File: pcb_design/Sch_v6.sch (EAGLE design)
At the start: 33 parts

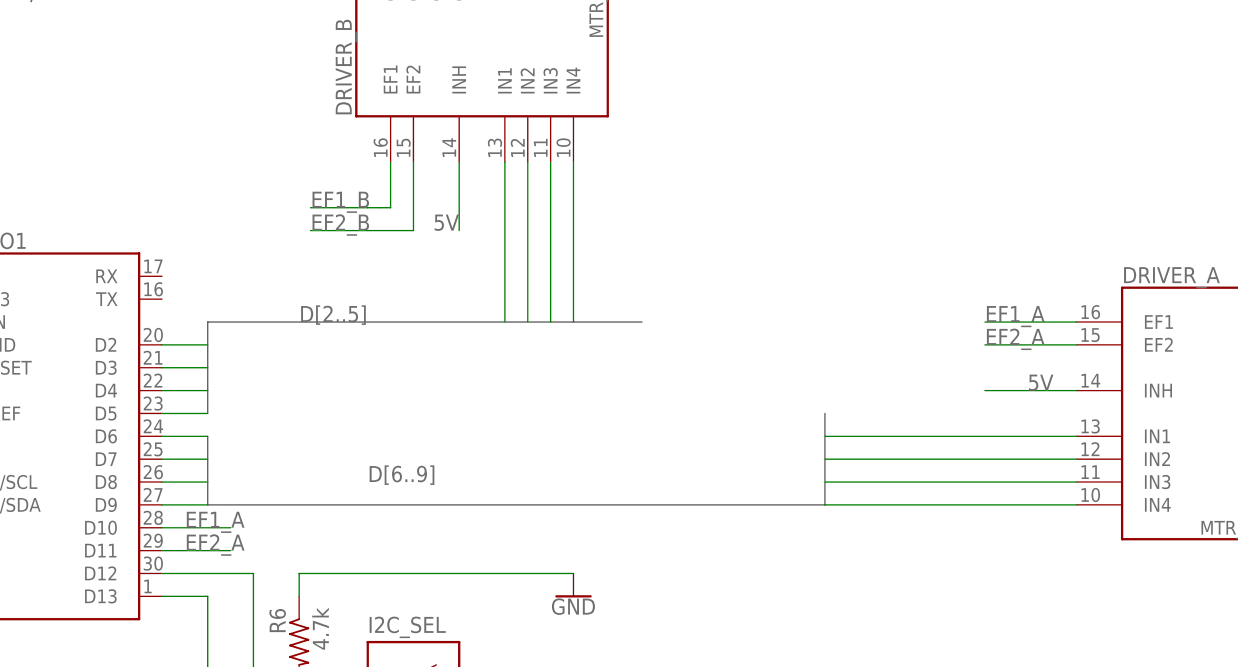
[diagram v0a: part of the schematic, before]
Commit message: removed old files and updated with CAM files for both pcbs.
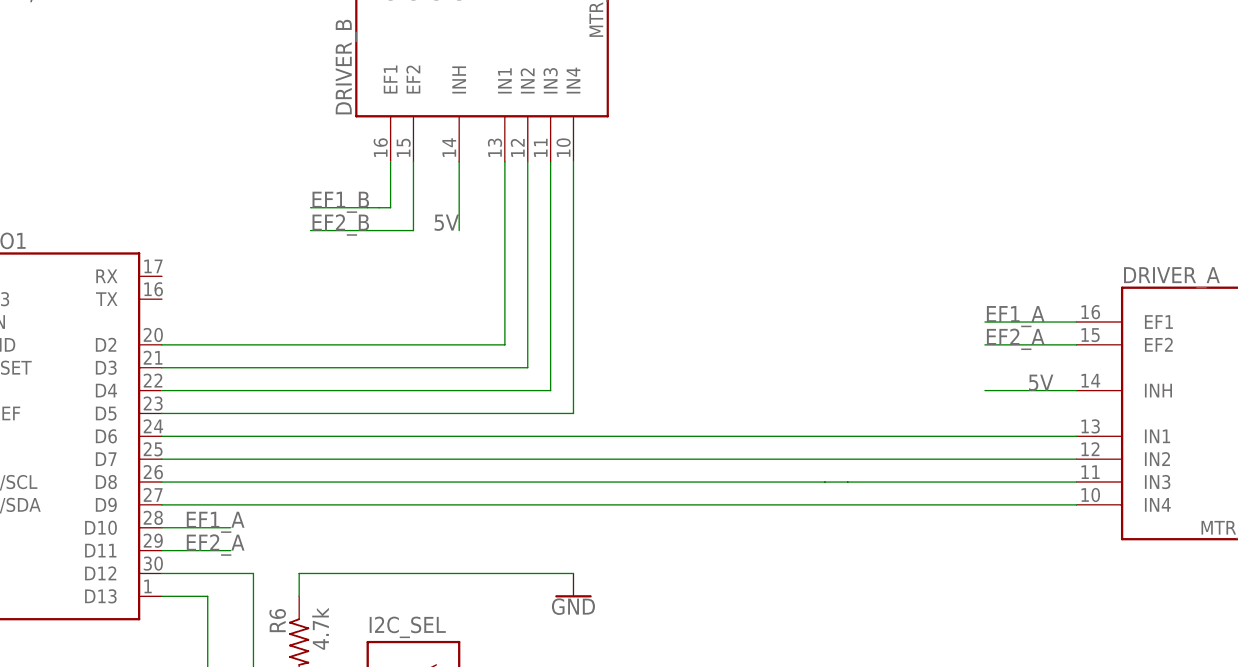
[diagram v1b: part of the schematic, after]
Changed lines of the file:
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@@
-</segment>
-</bus>
-<bus name="D[6..9]">
-<segment>
-<wire x1="53.34" y1="104.14" x2="53.34" y2="96.52" width="0.762" layer="92"/>
-<wire x1="53.34" y1="96.52" x2="121.92" y2="96.52" width="0.762" layer="92"/>
-<wire x1="121.92" y1="96.52" x2="121.92" y2="106.68" width="0.762" layer="92"/>
-<label x="71.12" y="99.06" size="1.778" layer="95"/>
-</segment>
-</bus>
-<bus name="D[2..5]">
-<segment>
-<wire x1="53.34" y1="106.68" x2="53.34" y2="116.84" width="0.762" layer="92"/>
-<wire x1="53.34" y1="116.84" x2="101.6" y2="116.84" width="0.762" layer="92"/>
-<label x="63.5" y="116.84" size="1.778" layer="95"/>
 </segment>
 </bus>
@@
 <net name="D6" class="0">
 <segment>
-<wire x1="149.86" y1="104.14" x2="121.92" y2="104.14" width="0.1524" layer="91"/>
+<pinref part="NANO1" gate="NANO_EVERY" pin="D6"/>
 <pinref part="DRIVER_A" gate="G$1" pin="IN1"/>
-</segment>
-<segment>
-<wire x1="48.26" y1="104.14" x2="53.34" y2="104.14" width="0.1524" layer="91"/>
-<pinref part="NANO1" gate="NANO_EVERY" pin="D6"/>
+<wire x1="48.26" y1="104.14" x2="149.86" y2="104.14" width="0.1524" layer="91"/>
 </segment>
 </net>
 <net name="D7" class="0">
 <segment>
-<wire x1="149.86" y1="101.6" x2="121.92" y2="101.6" width="0.1524" layer="91"/>
+<pinref part="NANO1" gate="NANO_EVERY" pin="D7"/>
 <pinref part="DRIVER_A" gate="G$1" pin="IN2"/>
-</segment>
-<segment>
-<wire x1="48.26" y1="101.6" x2="53.34" y2="101.6" width="0.1524" layer="91"/>
-<pinref part="NANO1" gate="NANO_EVERY" pin="D7"/>
+<wire x1="48.26" y1="101.6" x2="149.86" y2="101.6" width="0.1524" layer="91"/>
 </segment>
 </net>
 <net name="D8" class="0">
 <segment>
-<wire x1="149.86" y1="99.06" x2="121.92" y2="99.06" width="0.1524" layer="91"/>
+<pinref part="NANO1" gate="NANO_EVERY" pin="D8"/>
+<wire x1="149.86" y1="99.06" x2="124.46" y2="99.06" width="0.1524" layer="91"/>
 <pinref part="DRIVER_A" gate="G$1" pin="IN3"/>
-</segment>
-<segment>
-<wire x1="48.26" y1="99.06" x2="53.34" y2="99.06" width="0.1524" layer="91"/>
-<pinref part="NANO1" gate="NANO_EVERY" pin="D8"/>
+<wire x1="124.46" y1="99.06" x2="121.92" y2="99.06" width="0.1524" layer="91"/>
+<wire x1="48.26" y1="99.06" x2="121.92" y2="99.06" width="0.1524" layer="91"/>
 </segment>
 </net>
 <net name="D9" class="0">
 <segment>
-<wire x1="149.86" y1="96.52" x2="121.92" y2="96.52" width="0.1524" layer="91"/>
+<pinref part="NANO1" gate="NANO_EVERY" pin="D9"/>
 <pinref part="DRIVER_A" gate="G$1" pin="IN4"/>
-</segment>
-<segment>
-<wire x1="48.26" y1="96.52" x2="53.34" y2="96.52" width="0.1524" layer="91"/>
-<pinref part="NANO1" gate="NANO_EVERY" pin="D9"/>
+<wire x1="48.26" y1="96.52" x2="149.86" y2="96.52" width="0.1524" layer="91"/>
 </segment>
 </net>
 <net name="D2" class="0">
 <segment>
-<wire x1="86.36" y1="134.62" x2="86.36" y2="116.84" width="0.1524" layer="91"/>
+<pinref part="NANO1" gate="NANO_EVERY" pin="D2"/>
+<wire x1="86.36" y1="134.62" x2="86.36" y2="114.3" width="0.1524" layer="91"/>
 <pinref part="DRIVER_B" gate="G$1" pin="IN1"/>
-</segment>
-<segment>
-<wire x1="48.26" y1="114.3" x2="53.34" y2="114.3" width="0.1524" layer="91"/>
-<pinref part="NANO1" gate="NANO_EVERY" pin="D2"/>
+<wire x1="48.26" y1="114.3" x2="86.36" y2="114.3" width="0.1524" layer="91"/>
 </segment>
 </net>
 <net name="D3" class="0">
 <segment>
-<wire x1="88.9" y1="134.62" x2="88.9" y2="116.84" width="0.1524" layer="91"/>
+<pinref part="NANO1" gate="NANO_EVERY" pin="D3"/>
+<wire x1="88.9" y1="134.62" x2="88.9" y2="111.76" width="0.1524" layer="91"/>
 <pinref part="DRIVER_B" gate="G$1" pin="IN2"/>
-</segment>
-<segment>
-<wire x1="48.26" y1="111.76" x2="53.34" y2="111.76" width="0.1524" layer="91"/>
-<pinref part="NANO1" gate="NANO_EVERY" pin="D3"/>
+<wire x1="48.26" y1="111.76" x2="88.9" y2="111.76" width="0.1524" layer="91"/>
 </segment>
 </net>
 <net name="D4" class="0">
 <segment>
-<wire x1="91.44" y1="134.62" x2="91.44" y2="116.84" width="0.1524" layer="91"/>
+<pinref part="NANO1" gate="NANO_EVERY" pin="D4"/>
+<wire x1="91.44" y1="134.62" x2="91.44" y2="109.22" width="0.1524" layer="91"/>
 <pinref part="DRIVER_B" gate="G$1" pin="IN3"/>
-</segment>
-<segment>
-<wire x1="48.26" y1="109.22" x2="53.34" y2="109.22" width="0.1524" layer="91"/>
-<pinref part="NANO1" gate="NANO_EVERY" pin="D4"/>
+<wire x1="48.26" y1="109.22" x2="91.44" y2="109.22" width="0.1524" layer="91"/>
 </segment>
 </net>
 <net name="D5" class="0">
 <segment>
-<wire x1="93.98" y1="134.62" x2="93.98" y2="116.84" width="0.1524" layer="91"/>
+<pinref part="NANO1" gate="NANO_EVERY" pin="D5"/>
+<wire x1="93.98" y1="134.62" x2="93.98" y2="106.68" width="0.1524" layer="91"/>
 <pinref part="DRIVER_B" gate="G$1" pin="IN4"/>
-</segment>
-<segment>
-<wire x1="48.26" y1="106.68" x2="53.34" y2="106.68" width="0.1524" layer="91"/>
-<pinref part="NANO1" gate="NANO_EVERY" pin="D5"/>
-</segment>
-</net>
+<wire x1="48.26" y1="106.68" x2="93.98" y2="106.68" width="0.1524" layer="91"/>
+</segment>
+</net>
